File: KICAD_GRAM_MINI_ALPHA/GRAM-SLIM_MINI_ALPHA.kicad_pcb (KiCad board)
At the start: 2 copper layers, 216 x 135 mm, 64 parts, among them J1 USB C Connector, J2 JTAG_TC2030, SW1 Boot, U1 XC6206, U2 USBLC6-2SC6, U3 RP2040, U4 W25Q128JVS, Y1 12MHz

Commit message: flip side of USB connector
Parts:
- added R6: 10k, Resistor_SMD:R_0603_1608Metric, F.Cu at (1.50, 0.76)
- J1: moved to F.Cu
- moved R2 7.41 mm to (200.0, 46.2)
- moved R3 4.37 mm to (204.0, 52.6), turned to 0 degrees
- moved R1 1.17 mm to (195.5, 50.8)
- turned J1 to 180 degrees
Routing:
- net 3vCable: track 76.3 -> 60.8 mm, vias 3 -> 2
- net Net-(J1-CC2): track 16.0 -> 1.76 mm
- net DATA: track 72.6 -> 62.3 mm
- net C_RT: track 175.8 -> 169.7 mm
- net GND: track 50.3 -> 54.3 mm, vias 49 -> 84
- net Net-(J1-SHIELD): track 17.7 -> 21.2 mm
- net DBUS-: track 35.0 -> 37.4 mm, vias 2 -> 3
- net EXTRA: track 188.0 -> 186.1 mm
- net DOWN: track 171.8 -> 169.9 mm
- net A: track 195.0 -> 193.1 mm
- net M1: track 150.1 -> 148.2 mm
- net LEFT: track 200.3 -> 198.4 mm
- net C_UP: track 216.1 -> 214.2 mm
- net C_DN: track 198.5 -> 196.6 mm
- net START: track 103.8 -> 101.9 mm
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
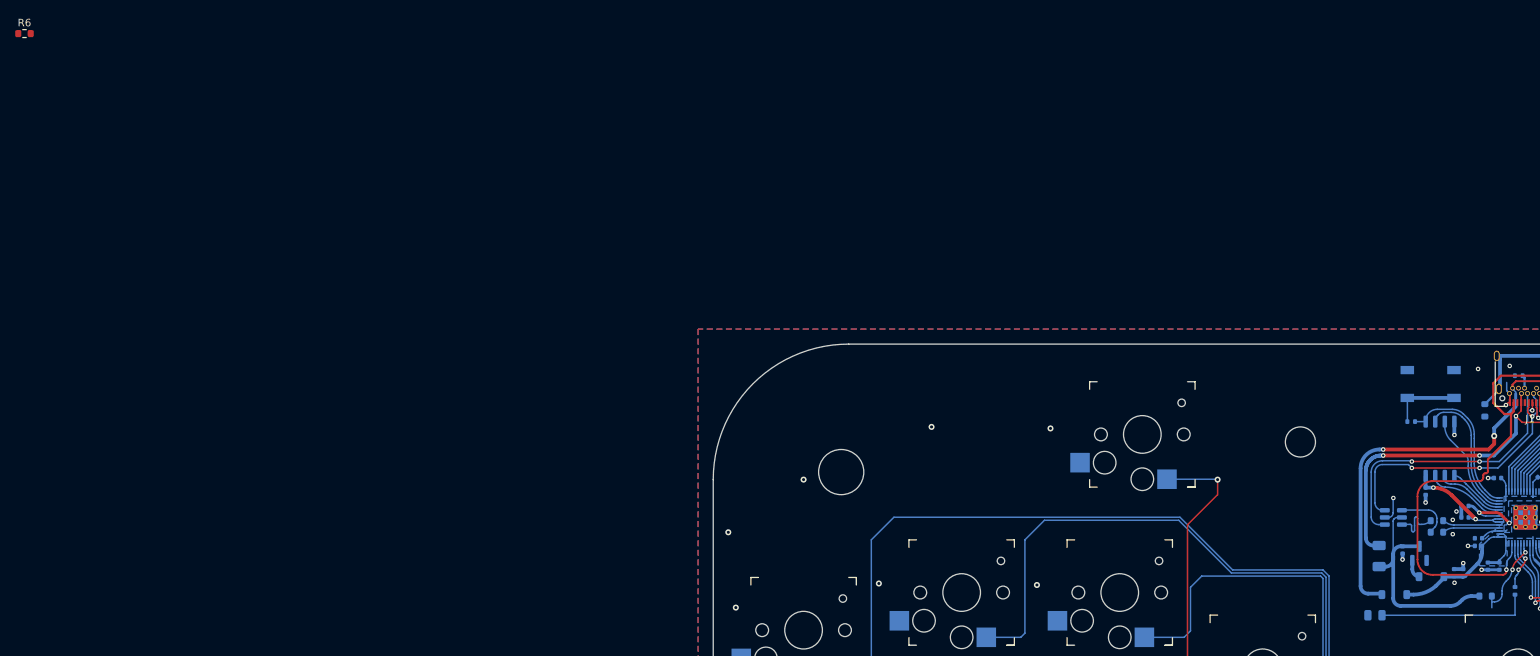
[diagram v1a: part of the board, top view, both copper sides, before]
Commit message: move resistor that wasn't placed
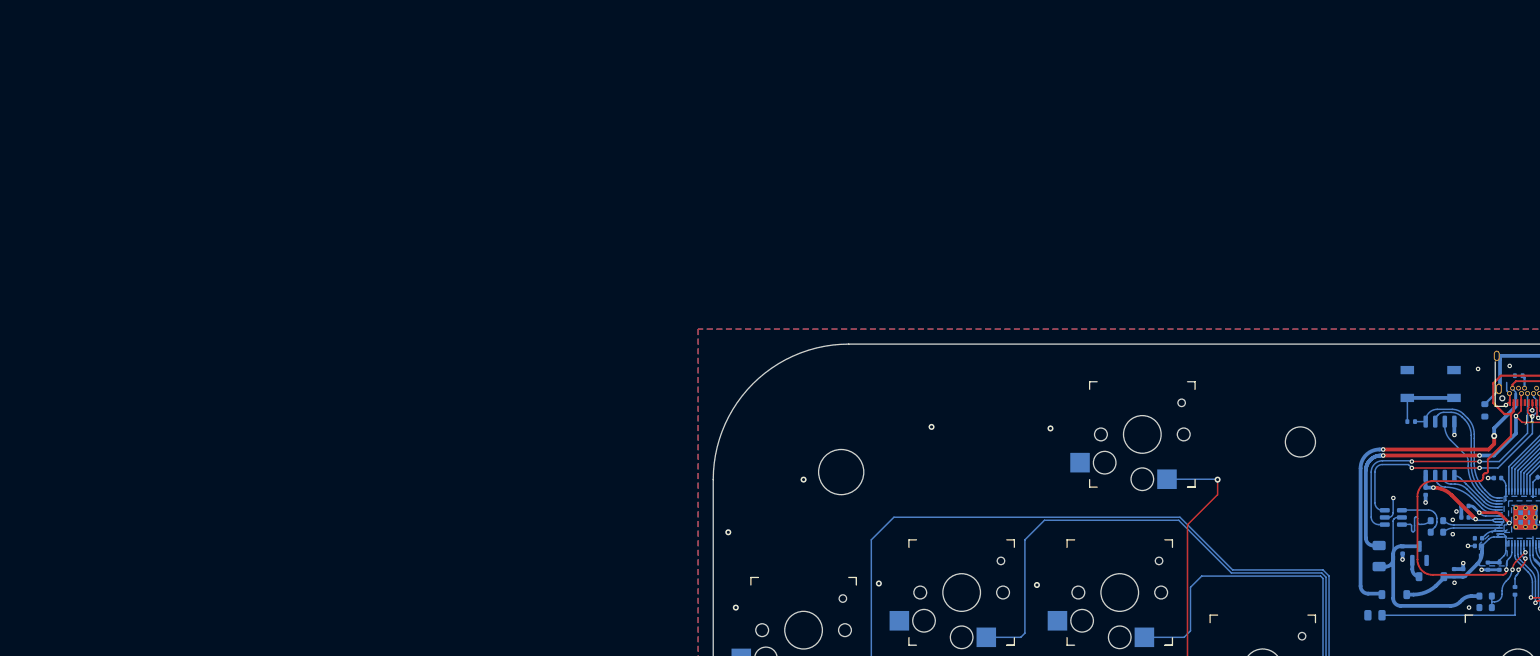
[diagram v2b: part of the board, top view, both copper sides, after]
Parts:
- R6: moved to B.Cu
- moved R6 208.5 mm to (195.6, 77.0), turned to 180 degrees
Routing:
- net GND: vias 84 -> 85
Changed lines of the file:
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@@
 	(net 66 "SD1")
 	(net 67 "EXTRA")
-	(footprint "Resistor_SMD:R_0603_1608Metric"
-		(layer "F.Cu")
-		(at 1.505 0.755)
-		(descr "Resistor SMD 0603 (1608 Metric), square (rectangular) end terminal, IPC-7351 nominal, (Body size source: IPC-SM-782 page 72, https://www.pcb-3d.com/wordpress/wp-content/uploads/ipc-sm-782a_amendment_1_and_2.pdf), generated with kicad-footprint-generator")
-		(tags "resistor")
-		(property "Reference" "R6"
-			(at 0 -1.43 0)
-			(layer "F.SilkS")
-			(effects
-				(font
-					(size 1 1)
-					(thickness 0.15)
-				)
-			)
-		)
-		(property "Value" "10k"
-			(at 0 1.43 0)
-			(layer "F.Fab")
-			(effects
-				(font
-					(size 1 1)
-					(thickness 0.15)
-				)
-			)
-		)
-		(property "Datasheet" "~"
-			(at 0 0 0)
-			(layer "F.Fab")
-			(hide yes)
-			(effects
-				(font
-					(size 1.27 1.27)
-					(thickness 0.15)
-				)
-			)
-		)
-		(property "Description" ""
-			(at 0 0 0)
-			(layer "F.Fab")
-			(hide yes)
-			(effects
-				(font
-					(size 1.27 1.27)
-					(thickness 0.15)
-				)
-			)
-		)
-		(property ki_fp_filters "R_*")
-		(sheetname "/")
-		(sheetfile "GRAM-SLIM_MINI_ALPHA.kicad_sch")
-		(attr smd)
-		(fp_line
-			(start -0.237258 -0.5225)
-			(end 0.237258 -0.5225)
-			(stroke
-				(width 0.12)
-				(type solid)
-			)
-			(layer "F.SilkS")
-		)
-		(fp_line
-			(start -0.237258 0.5225)
-			(end 0.237258 0.5225)
-			(stroke
-				(width 0.12)
-				(type solid)
-			)
-			(layer "F.SilkS")
-		)
-		(fp_line
-			(start -1.48 -0.73)
-			(end 1.48 -0.73)
-			(stroke
-				(width 0.05)
-				(type solid)
-			)
-			(layer "F.CrtYd")
-		)
-		(fp_line
-			(start -1.48 0.73)
-			(end -1.48 -0.73)
-			(stroke
-				(width 0.05)
-				(type solid)
-			)
-			(layer "F.CrtYd")
-		)
-		(fp_line
-			(start 1.48 -0.73)
-			(end 1.48 0.73)
-			(stroke
-				(width 0.05)
-				(type solid)
-			)
-			(layer "F.CrtYd")
-		)
-		(fp_line
-			(start 1.48 0.73)
-			(end -1.48 0.73)
-			(stroke
-				(width 0.05)
-				(type solid)
-			)
-			(layer "F.CrtYd")
-		)
-		(fp_line
-			(start -0.8 -0.4125)
-			(end 0.8 -0.4125)
-			(stroke
-				(width 0.1)
-				(type solid)
-			)
-			(layer "F.Fab")
-		)
-		(fp_line
-			(start -0.8 0.4125)
-			(end -0.8 -0.4125)
-			(stroke
-				(width 0.1)
-				(type solid)
-			)
-			(layer "F.Fab")
-		)
-		(fp_line
-			(start 0.8 -0.4125)
-			(end 0.8 0.4125)
-			(stroke
-				(width 0.1)
-				(type solid)
-			)
-			(layer "F.Fab")
-		)
-		(fp_line
-			(start 0.8 0.4125)
-			(end -0.8 0.4125)
-			(stroke
-				(width 0.1)
-				(type solid)
-			)
-			(layer "F.Fab")
-		)
-		(fp_text user "${REFERENCE}"
-			(at 0 0 0)
-			(layer "F.Fab")
-			(effects
-				(font
-					(size 0.4 0.4)
-					(thickness 0.06)
-				)
-			)
-		)
-		(pad "1" smd roundrect
-			(at -0.825 0)
-			(size 0.8 0.95)
-			(layers "F.Cu" "F.Mask" "F.Paste")
-			(roundrect_rratio 0.25)
-			(net 28 "VBUS_SENSE")
-			(pintype "passive")
-		)
-		(pad "2" smd roundrect
-			(at 0.825 0)
-			(size 0.8 0.95)
-			(layers "F.Cu" "F.Mask" "F.Paste")
-			(roundrect_rratio 0.25)
-			(net 1 "GND")
-			(pintype "passive")
-		)
-		(embedded_fonts no)
-		(model "${KICAD9_3DMODEL_DIR}/Resistor_SMD.3dshapes/R_0603_1608Metric.step"
-			(offset
-				(xyz 0 0 0)
-			)
-			(scale
-				(xyz 1 1 1)
-			)
-			(rotate
-				(xyz 0 0 0)
-			)
-		)
-	)
 	(footprint "MicroGRAM:Kailh_socket_PG1350"
 		(layer "F.Cu")
@@
 		)
 	)
+	(footprint "Resistor_SMD:R_0603_1608Metric"
+		(layer "B.Cu")
+		(at 195.6 77 180)
+		(descr "Resistor SMD 0603 (1608 Metric), square (rectangular) end terminal, IPC-7351 nominal, (Body size source: IPC-SM-782 page 72, https://www.pcb-3d.com/wordpress/wp-content/uploads/ipc-sm-782a_amendment_1_and_2.pdf), generated with kicad-footprint-generator")
+		(tags "resistor")
+		(property "Reference" "R6"
+			(at 0 1.43 0)
+			(layer "B.SilkS")
+			(effects
+				(font
+					(size 1 1)
+					(thickness 0.15)
+				)
+				(justify mirror)
+			)
+		)
+		(property "Value" "10k"
+			(at 0 -1.43 0)
+			(layer "B.Fab")
+			(effects
+				(font
+					(size 1 1)
+					(thickness 0.15)
+				)
+				(justify mirror)
+			)
+		)
+		(property "Datasheet" "~"
+			(at 0 0 0)
+			(layer "B.Fab")
+			(hide yes)
+			(effects
+				(font
+					(size 1.27 1.27)
+					(thickness 0.15)
+				)
+				(justify mirror)
+			)
+		)
+		(property "Description" ""
+			(at 0 0 0)
+			(layer "B.Fab")
+			(hide yes)
+			(effects
+				(font
+					(size 1.27 1.27)
+					(thickness 0.15)
+				)
+				(justify mirror)
+			)
+		)
+		(property ki_fp_filters "R_*")
+		(sheetname "/")
+		(sheetfile "GRAM-SLIM_MINI_ALPHA.kicad_sch")
+		(attr smd)
+		(fp_line
+			(start -0.237258 0.5225)
+			(end 0.237258 0.5225)
+			(stroke
+				(width 0.12)
+				(type solid)
+			)
+			(layer "B.SilkS")
+		)
+		(fp_line
+			(start -0.237258 -0.5225)
+			(end 0.237258 -0.5225)
+			(stroke
+				(width 0.12)
+				(type solid)
+			)
+			(layer "B.SilkS")
+		)
+		(fp_line
+			(start 1.48 0.73)
+			(end 1.48 -0.73)
+			(stroke
+				(width 0.05)
+				(type solid)
+			)
+			(layer "B.CrtYd")
+		)
+		(fp_line
+			(start 1.48 -0.73)
+			(end -1.48 -0.73)
+			(stroke
+				(width 0.05)
+				(type solid)
+			)
+			(layer "B.CrtYd")
+		)
+		(fp_line
+			(start -1.48 0.73)
+			(end 1.48 0.73)
+			(stroke
+				(width 0.05)
+				(type solid)
+			)
+			(layer "B.CrtYd")
+		)
+		(fp_line
+			(start -1.48 -0.73)
+			(end -1.48 0.73)
+			(stroke
+				(width 0.05)
+				(type solid)
+			)
+			(layer "B.CrtYd")
+		)
+		(fp_line
+			(start 0.8 0.4125)
+			(end 0.8 -0.4125)
+			(stroke
+				(width 0.1)
+				(type solid)
+			)
+			(layer "B.Fab")
+		)
+		(fp_line
+			(start 0.8 -0.4125)
+			(end -0.8 -0.4125)
+			(stroke
+				(width 0.1)
+				(type solid)
+			)
+			(layer "B.Fab")
+		)
+		(fp_line
+			(start -0.8 0.4125)
+			(end 0.8 0.4125)
+			(stroke
+				(width 0.1)
+				(type solid)
+			)
+			(layer "B.Fab")
+		)
+		(fp_line
+			(start -0.8 -0.4125)
+			(end -0.8 0.4125)
+			(stroke
+				(width 0.1)
+				(type solid)
+			)
+			(layer "B.Fab")
+		)
+		(fp_text user "${REFERENCE}"
+			(at 0 0 0)
+			(layer "B.Fab")
+			(effects
+				(font
+					(size 0.4 0.4)
+					(thickness 0.06)
+				)
+				(justify mirror)
+			)
+		)
+		(pad "1" smd roundrect
+			(at -0.825 0 180)
+			(size 0.8 0.95)
+			(layers "B.Cu" "B.Mask" "B.Paste")
+			(roundrect_rratio 0.25)
+			(net 28 "VBUS_SENSE")
+			(pintype "passive")
+		)
+		(pad "2" smd roundrect
+			(at 0.825 0 180)
+			(size 0.8 0.95)
+			(layers "B.Cu" "B.Mask" "B.Paste")
+			(roundrect_rratio 0.25)
+			(net 1 "GND")
+			(pintype "passive")
+		)
+		(embedded_fonts no)
+		(model "${KICAD9_3DMODEL_DIR}/Resistor_SMD.3dshapes/R_0603_1608Metric.step"
+			(offset
+				(xyz 0 0 0)
+			)
+			(scale
+				(xyz 1 1 1)
+			)
+			(rotate
+				(xyz 0 0 0)
+			)
+		)
+	)
 	(footprint "Capacitor_SMD:C_0402_1005Metric"
 		(layer "B.Cu")
@@
 		(tags "capacitor")
 		(property "Reference" "C16"
-			(at 1.883 -0.00975 90)
+			(at 1.883 -0.00975 180)
 			(layer "B.SilkS")
 			(effects
@@
 	)
 	(via
+		(at 193.4 77)
+		(size 0.6)
+		(drill 0.3)
+		(layers "F.Cu" "B.Cu")
+		(free yes)
+		(net 1)
+	)
+	(via
 		(at 239 74)
 		(size 0.8)
@@
 		(width 0.2)
 		(layer "B.Cu")
-		(net 47)
-	)
-	(segment
-		(start 227 114)
-		(end 227 114)
-		(width 0.2)
-		(layer "B.Cu")
